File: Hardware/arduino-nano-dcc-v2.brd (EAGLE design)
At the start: 100 x 80 mm, 40 parts, among them IC1 7805TV, IC2 7805TV, IC3 MEGA328-P, X1 22-23-2031

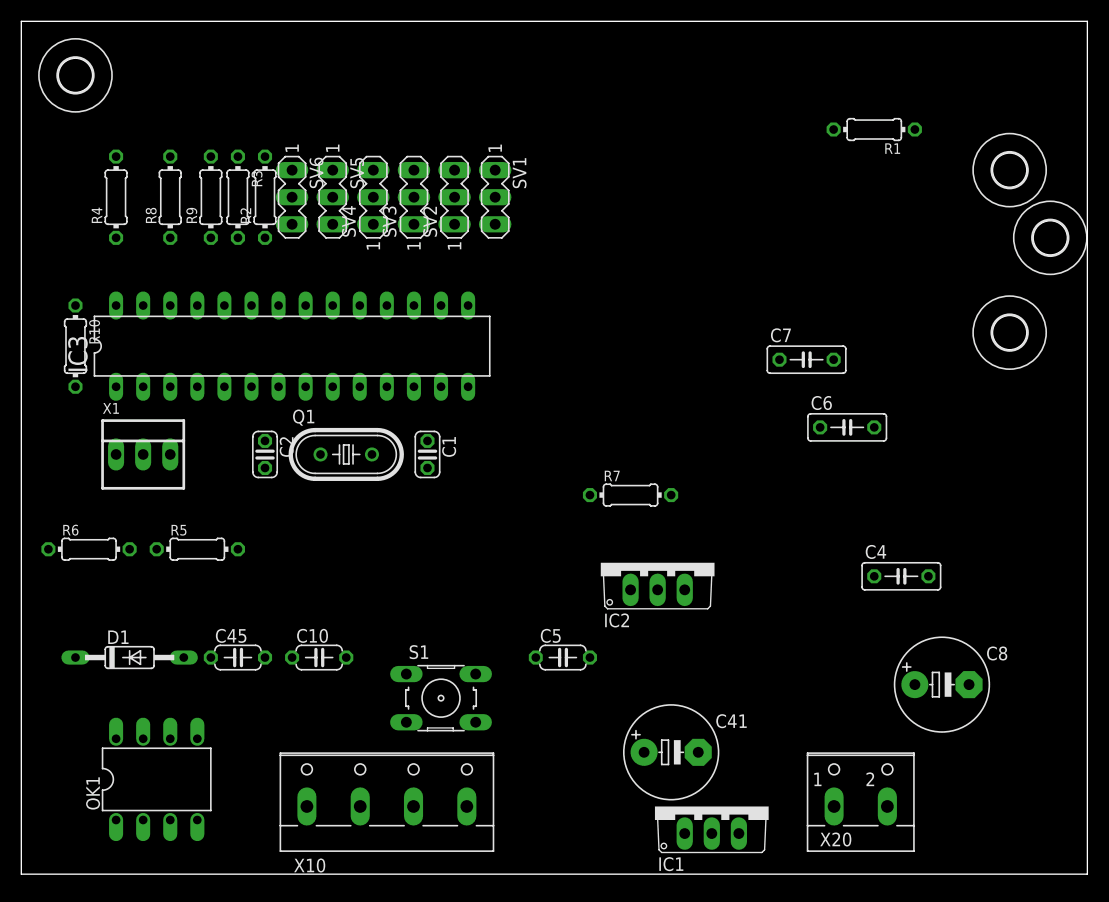
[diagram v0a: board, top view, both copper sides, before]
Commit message: Changes  * Added TIP for 5V supply servo's,  * Initial routing.
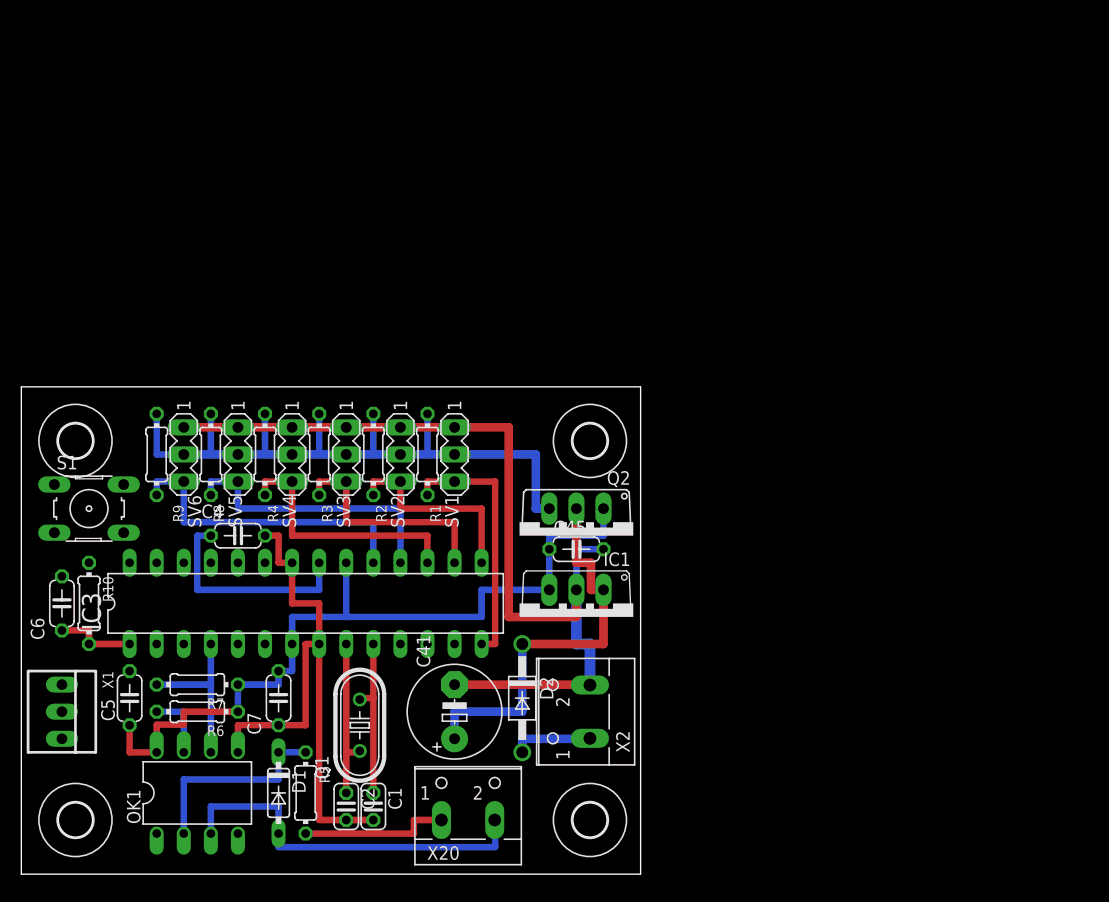
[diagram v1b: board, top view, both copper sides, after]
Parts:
- removed C10: 100n, rcl:C050-024X044
- removed C8: 220uF 25V, rcl:E5-8,5
- removed IC2: 7805TV, linear:TO220V
- removed X10: (no value), con-wago-500:W237-4
- added D2: 1N4004, diode:DO41-10
- added Q2: TIP41C, transistor-power:TO220AV
- added X2: (no value), con-wago-500:W237-102
- C4, C6, C7: device rcl:C050-025X075 -> rcl:C050-024X044
- D1: device diode:DO35-10 -> diode:DO35-7
- moved H4 98.8 mm to (5.08, 5.08)
- moved C6 75.5 mm to (3.81, 25.4), turned to 90 degrees
- moved H3 69.6 mm to (53.3, 5.08)
- moved C4 62.3 mm to (20.3, 31.8)
- moved C7 58.8 mm to (24.1, 16.5), turned to 90 degrees
- moved R1 51.8 mm to (38.1, 39.4), turned to 90 degrees
- moved H2 46.9 mm to (53.3, 40.6)
- moved R7 44.4 mm to (16.5, 17.8), turned to 180 degrees
- moved C5 40.8 mm to (10.2, 16.5), turned to 90 degrees
- moved S1 37.5 mm to (6.35, 34.3)
- moved X20 36.9 mm to (41.9, 6.35)
- moved H1 34.3 mm to (5.08, 40.6)
- moved C2 33.9 mm to (30.5, 6.35)
- moved C1 33.4 mm to (33.0, 6.35)
- moved C45 33.3 mm to (52.1, 30.5)
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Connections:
- net +5V: now also Q2.B
- net +5V/2: now also Q2.E; no longer C10.1, IC2.3
- net GND: now also X2.2; no longer C10.2, C8.-, IC2.2, X10.1, X10.2
- net N$1: now also D2.C, Q2.C; no longer X10.3, X10.4
- net N$2: now also D2.A, X2.1; no longer C8.+, IC2.1
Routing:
- net GND: track 0.00 -> 142.4 mm
- net +5V/2: track 0.00 -> 77.5 mm
- net +5V: track 0.00 -> 74.9 mm
- net N$1: track 0.00 -> 38.1 mm
- net N$19: track 0.00 -> 35.6 mm
- net SERVO6: track 0.00 -> 29.2 mm
- net SERVO5: track 0.00 -> 26.7 mm
- net SERVO1: track 0.00 -> 24.1 mm
- net SERVO4: track 0.00 -> 24.1 mm
- net SERVO3: track 0.00 -> 21.6 mm
- net N$6: track 0.00 -> 20.3 mm
- net N$17: track 0.00 -> 19.1 mm
- net SERVO2: track 0.00 -> 19.0 mm
- net N$4: track 0.00 -> 15.4 mm
- net N$3: track 0.00 -> 15.4 mm
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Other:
- board size 100 x 80 mm -> 58.1 x 45.7 mm

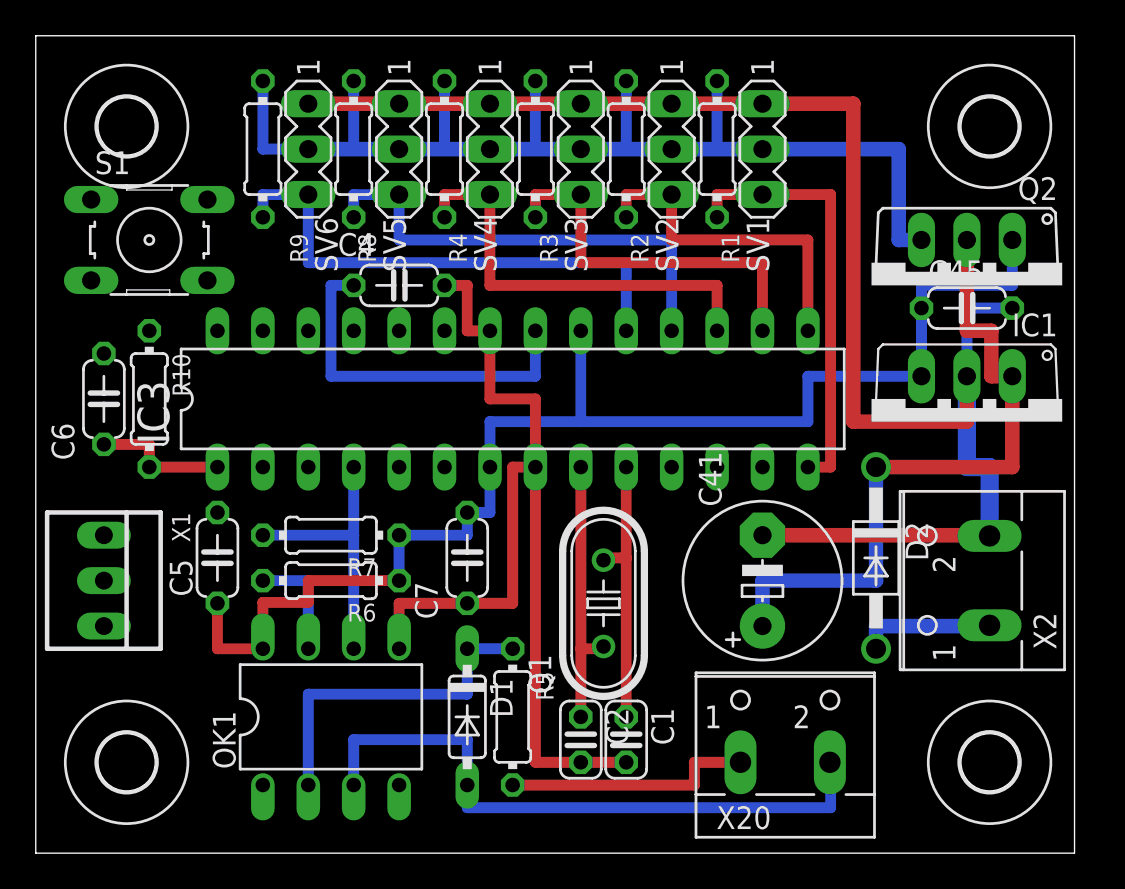
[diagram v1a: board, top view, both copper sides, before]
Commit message: Changes :  * Last traces routed.  * Extended to 8 servo's  * PCB somewhat bigger so 8 servo connections fit between the mounting holes.
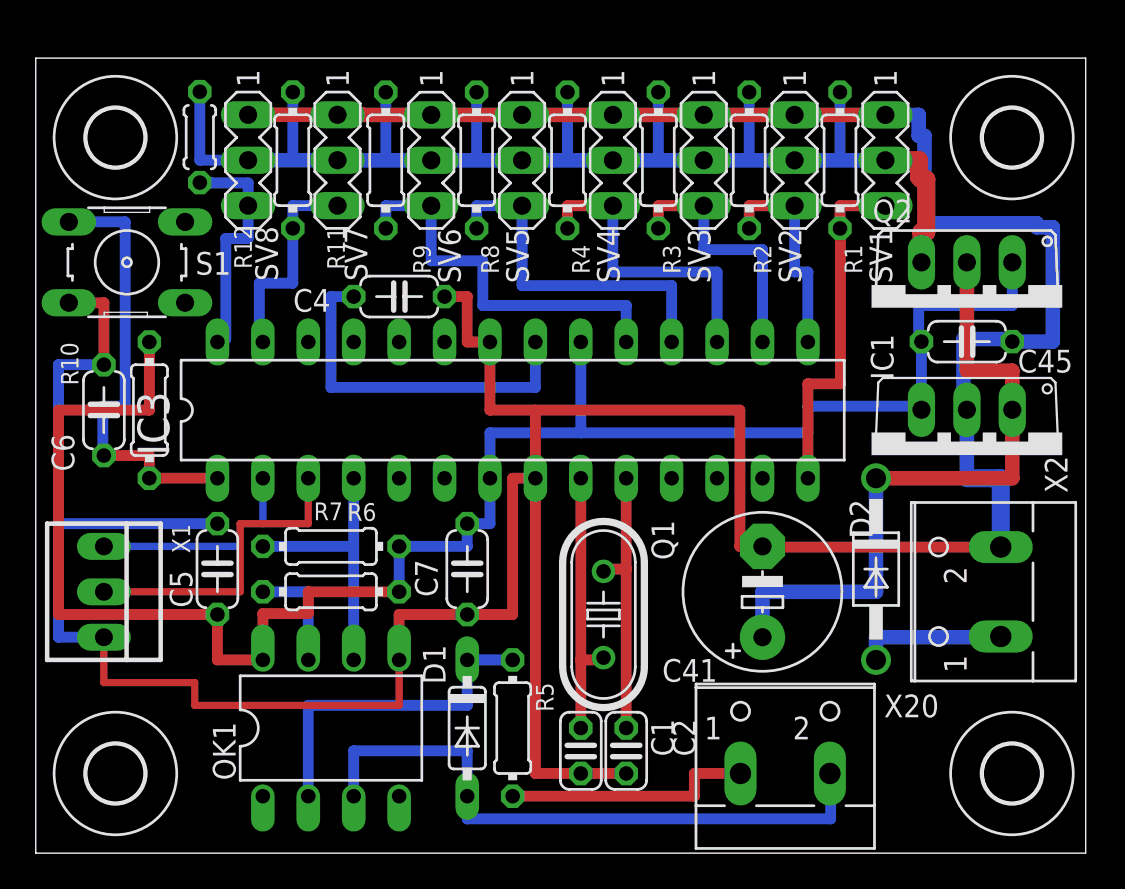
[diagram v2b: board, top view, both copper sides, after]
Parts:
- added R11: 4k7, rcl:0204/7
- added R12: 4k7, rcl:0204/5
- added SV7, SV8: (no value), con-lstb:MA03-1
- moved R1 6.90 mm to (45.0, 38.7)
- moved R2 6.90 mm to (39.9, 38.7)
- moved R4 6.90 mm to (29.7, 38.7)
- moved R8 6.90 mm to (24.7, 38.7)
- moved R9 6.90 mm to (19.6, 38.7)
- moved SV1 6.90 mm to (47.5, 38.7)
- moved SV2 6.90 mm to (42.4, 38.7)
- moved SV4 6.90 mm to (32.3, 38.7)
- moved SV5 6.90 mm to (27.2, 38.7)
- moved SV6 6.90 mm to (22.1, 38.7)
- moved R3 6.90 mm to (34.8, 38.7)
- moved SV3 6.90 mm to (37.4, 38.7)
- moved C45 1.88 mm to (52.1, 28.6)
- moved IC1 1.88 mm to (52.1, 22.3)
- moved S1 1.77 mm to (5.10, 33.0)
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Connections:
- new net SERVO7: IC3.27, R11.2, SV7.3
- new net SERVO8: IC3.28, R12.2, SV8.3
- net +5V/2: now also R11.1, R12.1, SV7.2, SV8.2
- net GND: now also SV7.1, SV8.1
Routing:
- net GND: track 142.4 -> 222.3 mm
- net +5V: track 74.9 -> 104.2 mm
- net TX: track 0.00 -> 17.8 mm
- net N$5: track 7.62 -> 25.1 mm
- net +5V/2: track 77.5 -> 94.8 mm
- net SERVO8: track 0.00 -> 13.3 mm
- net RX: track 0.00 -> 12.7 mm
- net SERVO7: track 0.00 -> 12.2 mm
- net SERVO5: track 26.7 -> 19.8 mm
- net SERVO4: track 24.1 -> 17.3 mm
- net SERVO2: track 19.0 -> 12.2 mm
- net SERVO6: track 29.2 -> 22.3 mm
- net SERVO3: track 21.6 -> 14.7 mm
- net SERVO1: track 24.1 -> 19.6 mm
- net N$1: track 38.1 -> 37.5 mm
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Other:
- board size 58.1 x 45.7 mm -> 58.7 x 44.5 mm
